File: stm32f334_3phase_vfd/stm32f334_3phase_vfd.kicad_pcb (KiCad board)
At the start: 2 copper layers, 120 x 70 mm, 65 parts, among them J1 HV, J2 PHA, J201 Conn_02x01, J202 Conn_02x01, J204 TP_IA, J205 Conn_02x01, J206 TP_VBU, J207 TP_VBV, J208 TP_VBW, J209 Conn_02x01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

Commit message: move 3 phase current sensors on a new board, allow for the current sense board to be stacked
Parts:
- removed C204, C213, C221: 100n, Capacitor_SMD:C_1206_3216Metric
- removed J204: TP_IA, Connector_PinHeader_2.54mm:PinHeader_1x01_P2.54mm_Vertical
- removed J211: TP_IB, Connector_PinHeader_2.54mm:PinHeader_1x01_P2.54mm_Vertical
- removed J217: TP_IC, Connector_PinHeader_2.54mm:PinHeader_1x01_P2.54mm_Vertical
- removed U202, U203, U204: CC6903SO-x0A, Package_SO:SO-8_3.9x4.9mm_P1.27mm
- added J10: MH, MountingHole:MountingHole_3.2mm_M3_Pad_TopBottom, F.Cu at (124.4, 103.2)
- added J11: MH, MountingHole:MountingHole_3.2mm_M3_Pad_TopBottom, F.Cu at (124.5, 41.2)
- added J12: Conn_01x06, Connector_JST:JST_PH_B6B-PH-K_1x06_P2.00mm_Vertical, F.Cu at (140.5, 93.6)
- C201, C203, C211, C212, C214, C215, C220, R202, R204, R206, R208, R211, R213: moved to B.Cu
- moved R203 213.3 mm to (150.8, 73.1), turned to 180 degrees
- moved C201 209.0 mm to (141.5, 75.5), turned to 180 degrees
- moved R205 207.3 mm to (150.8, 70.7), turned to 180 degrees
- moved R211 206.5 mm to (151.5, 62.9), turned to 180 degrees
- moved C203 205.6 mm to (141.5, 73.1), turned to 180 degrees
- moved J213 202.0 mm to (150.1, 53.5)
- moved R207 201.6 mm to (150.8, 66.6), turned to 180 degrees
- moved R204 201.0 mm to (151.5, 74.4), turned to 180 degrees
- moved C211 199.7 mm to (141.5, 70.7), turned to 180 degrees
- moved C215 197.5 mm to (141.5, 58.9), turned to 180 degrees
- moved R209 196.0 mm to (150.8, 64.2), turned to 180 degrees
- moved R208 195.3 mm to (151.5, 66.6), turned to 180 degrees
- moved C212 194.0 mm to (141.5, 66.6), turned to 180 degrees
- moved R210 192.2 mm to (155.7, 51.1), turned to 90 degrees
- moved R212 191.0 mm to (150.8, 61.8), turned to 180 degrees
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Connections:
- C205 pad 1: Net-(C205-Pad1) -> /power/OUTPUT_PH_W
- C207 pad 1: Net-(C207-Pad1) -> /power/OUTPUT_PH_V
- C209 pad 1: Net-(C209-Pad1) -> /power/OUTPUT_PH_U
- J2 pad 1: /power/OUTPUT_PHA -> /power/OUTPUT_PH_U
- J3 pad 1: /power/OUTPUT_PHB -> /power/OUTPUT_PH_V
- J4 pad 1: /power/OUTPUT_PHC -> /power/OUTPUT_PH_W
- U201 pad 21: Net-(C205-Pad1) -> /power/OUTPUT_PH_W
- U201 pad 22: Net-(C207-Pad1) -> /power/OUTPUT_PH_V
- U201 pad 23: Net-(C209-Pad1) -> /power/OUTPUT_PH_U
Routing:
- net GND: track 103.8 -> 2.17 mm, vias 3 -> 8
- net /power/3V3_ISENS: track 80.9 -> 0.00 mm, vias 3 -> 0
- net Net-(C205-Pad1): track 36.5 -> 0.00 mm, vias 2 -> 0
- net Net-(C209-Pad1): track 36.5 -> 0.00 mm, vias 2 -> 0
- net /CPU/ISENSE_C: track 36.1 -> 0.00 mm, vias 1 -> 0
- net Net-(C207-Pad1): track 33.7 -> 0.00 mm, vias 2 -> 0
- net /CPU/ISENSE_B: track 26.3 -> 0.00 mm, vias 1 -> 0
- net /power/VCC_15V: track 0.00 -> 16.1 mm
- net /power/OUTPUT_PHB: track 14.9 -> 0.00 mm
- net /power/OUTPUT_PHC: track 14.9 -> 0.00 mm
- net /power/OUTPUT_PHA: track 14.9 -> 0.00 mm
- net /CPU/ISENSE_A: track 14.8 -> 0.00 mm
- net /power/~{sd}_od: track 0.00 -> 14.3 mm
- net Net-(J201-Pad2): track 0.00 -> 7.34 mm
- net Net-(J215-Pad2): track 0.00 -> 7.32 mm
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- added copper zone on B.Cu, net /power/HV
- added copper zone on F.Cu, net /power/HV
- added copper zone on B.Cu, net /power/N
- added copper zone on B.Cu, net /power/OUTPUT_PH_U
- added copper zone on F.Cu, net /power/OUTPUT_PH_U
- added copper zone on B.Cu, net /power/OUTPUT_PH_V
- added copper zone on F.Cu, net /power/OUTPUT_PH_V
- added copper zone on B.Cu, net /power/OUTPUT_PH_W
- added copper zone on F.Cu, net /power/OUTPUT_PH_W
- added copper zone on B.Cu, net GND
- added copper zone on F.Cu, net GND
- removed copper zone on F.Cu, net /power/OUTPUT_PHA
- removed copper zone on F.Cu, net /power/OUTPUT_PHB
- removed copper zone on F.Cu, net /power/OUTPUT_PHC
- removed copper zone on F.Cu, net Net-(C205-Pad1)
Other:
- board text added: "A"
- board text added: "B"
- board text added: "C"
- board text added: "ES"
- board text added: "GND BOND POINT"
- board text added: "HIGH VOLTAGE"
- board text added: "HU"
- board text added: "HV"
- board text added: "HW"
- board text added: "LU"
- board text added: "LV"
- board text added: "LW"
- board text added: "POWER GND"
- board text added: "POWER VCC"

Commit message: switch to LQFP48 cpu, continue workin on layout
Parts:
- added C101: 8p, Capacitor_SMD:C_0805_2012Metric, F.Cu at (186.0, 75.4)
- added C102: 8p, Capacitor_SMD:C_0805_2012Metric, F.Cu at (188.9, 72.7)
- added C107: 100n, Capacitor_SMD:C_0805_2012Metric, F.Cu at (194.8, 57.0)
- added C108: 100n, Capacitor_SMD:C_0805_2012Metric, F.Cu at (194.9, 54.0)
- added C109: 100n, Capacitor_SMD:C_0805_2012Metric, F.Cu at (190.3, 59.8)
- added C110: 100n, Capacitor_SMD:C_0805_2012Metric, F.Cu at (190.3, 56.7)
- added C111: 100n, Capacitor_SMD:C_0805_2012Metric, F.Cu at (199.3, 54.0)
- added L101: FB, Inductor_SMD:L_0805_2012Metric, F.Cu at (190.4, 53.9)
- added U100: STM32F334C8Tx, Package_QFP:LQFP-48_7x7mm_P0.5mm, F.Cu at (174.4, 72.2)
- C202: value 330nF/630V -> B32774X8305K000; footprint Capacitor_THT:C_Rect_L24.0mm_W10.1mm_P22.50mm_MKT -> Capacitor_THT:C_Rect_L31.5mm_W11.0mm_P27.50mm_MKS4
- U101: value STM32F334K6Tx -> ECS-160-10-36-CKM-TR3; footprint Package_QFP:LQFP-32_7x7mm_P0.8mm -> Crystal:Crystal_SMD_2520-4Pin_2.5x2.0mm
- moved J207 215.5 mm to (142.4, 82.0), turned to 90 degrees
- moved J208 203.9 mm to (142.4, 78.4), turned to 90 degrees
- moved J206 201.0 mm to (142.4, 85.6), turned to 90 degrees
- moved U101 133.2 mm to (186.0, 72.7)
- moved J1 3.40 mm to (93.2, 89.5)
- moved J4 2.30 mm to (93.2, 62.7)
- moved J2 2.20 mm to (93.2, 75.2)
- moved C202 2.11 mm to (108.6, 58.6)
- moved R216 1.96 mm to (110.5, 54.1)
- moved C222 1.96 mm to (109.0, 47.3)
- moved R214 1.96 mm to (112.6, 48.8)
- moved R215 1.96 mm to (109.0, 44.8)
- moved R217 1.96 mm to (107.5, 50.3)
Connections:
- U101 pad 1: unconnected-(U101-Pad1) -> Net-(U100-Pad5)
- U101 pad 2: unconnected-(U101-Pad2) -> GND
- U101 pad 3: unconnected-(U101-Pad3) -> Net-(U100-Pad6)
- U101 pad 4: unconnected-(U101-Pad4) -> GND
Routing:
- net /CPU/L_V: track 0.00 -> 21.0 mm, vias 0 -> 1
- net /CPU/L_W: track 0.00 -> 19.5 mm
- net /CPU/H_U: track 0.00 -> 17.7 mm, vias 0 -> 1
- net /CPU/L_U: track 0.00 -> 15.1 mm
- net /CPU/H_V: track 0.00 -> 12.6 mm
- net /CPU/H_W: track 0.00 -> 12.3 mm, vias 0 -> 2
- net GND: track 2.17 -> 5.57 mm, vias 8 -> 18
- net GNDPWR: track 0.00 -> 2.91 mm
- net /power/Cin: track 42.0 -> 42.8 mm
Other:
- board text added: "VbU"
- board text added: "VbV"
- board text added: "VbW"

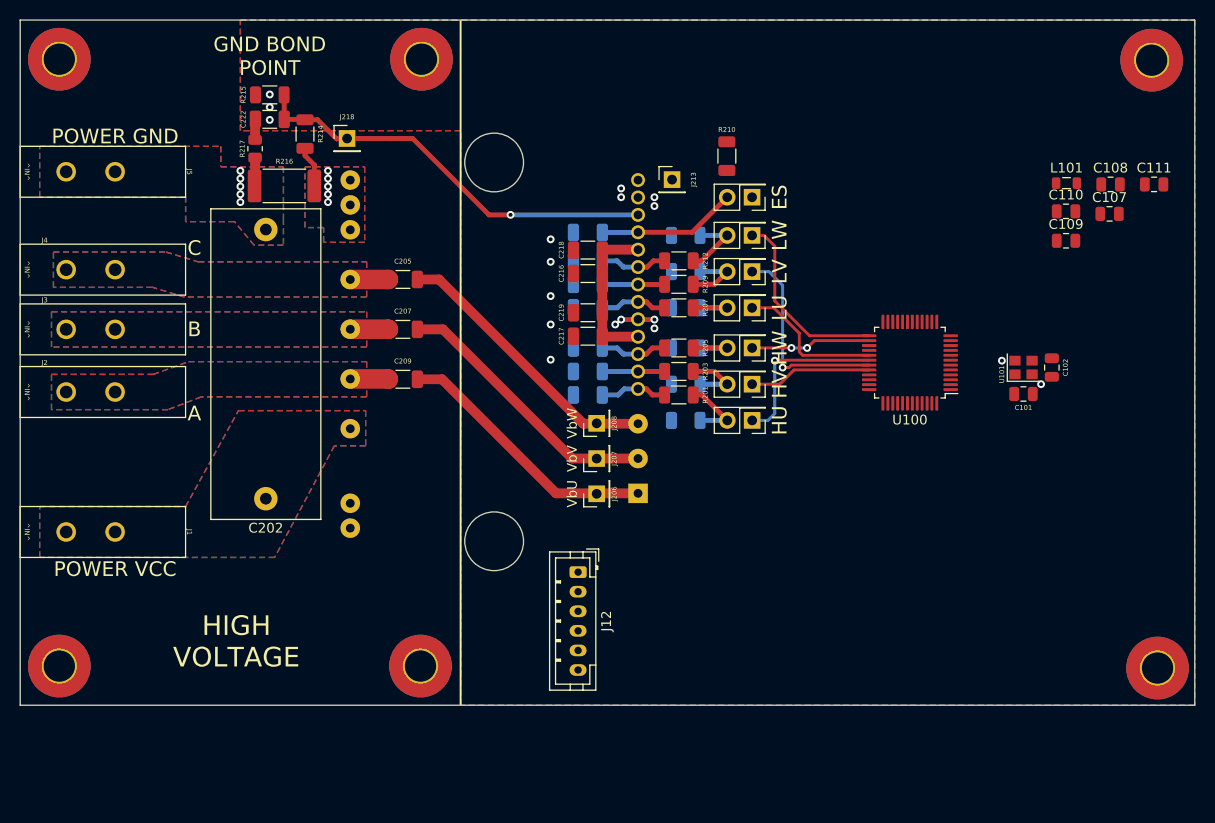
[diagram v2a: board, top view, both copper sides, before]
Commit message: pcb fix and schematic clean-up
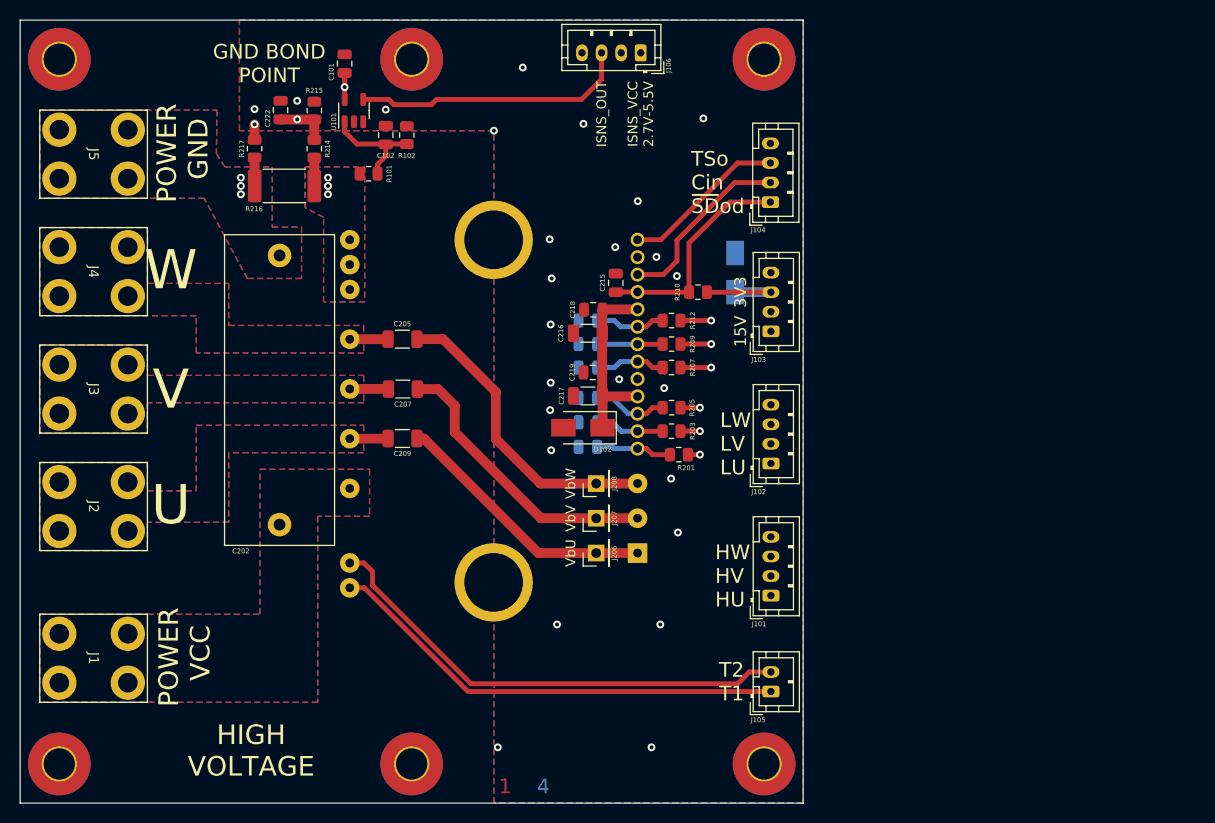
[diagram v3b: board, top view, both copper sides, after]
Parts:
- removed C107, C108, C109, C110, C111: 100n, Capacitor_SMD:C_0805_2012Metric
- removed J12: Conn_01x06, Connector_JST:JST_PH_B6B-PH-K_1x06_P2.00mm_Vertical
- removed J201, J202, J205, J209, J212, J214, J215: Conn_02x01, Connector_PinHeader_2.54mm:PinHeader_2x01_P2.54mm_Vertical
- removed J213: TP_TSO, Connector_PinHeader_2.54mm:PinHeader_1x01_P2.54mm_Vertical
- removed J218: TP_CSENSE, Connector_PinHeader_2.54mm:PinHeader_1x01_P2.54mm_Vertical
- removed L101: FB, Inductor_SMD:L_0805_2012Metric
- removed R202, R204, R206, R208, R211, R213: 10k, Resistor_SMD:R_1206_3216Metric
- removed U100: STM32F334C8Tx, Package_QFP:LQFP-48_7x7mm_P0.5mm
- added D101: D, Diode_SMD:D_SMA, B.Cu at (156.6, 63.0)
- added D102: D, Diode_SMD:D_SMA, F.Cu at (141.0, 78.8)
- added J101: Conn_01x04, Connector_JST:JST_PH_B4B-PH-K_1x04_P2.00mm_Vertical, F.Cu at (160.2, 96.0)
- added J102: Conn_01x04, Connector_JST:JST_PH_B4B-PH-K_1x04_P2.00mm_Vertical, F.Cu at (160.2, 82.5)
- added J103: Conn_01x04, Connector_JST:JST_PH_B4B-PH-K_1x04_P2.00mm_Vertical, F.Cu at (160.2, 69.0)
- added J104: Conn_01x04, Connector_JST:JST_PH_B4B-PH-K_1x04_P2.00mm_Vertical, F.Cu at (160.2, 55.8)
- added J105: Conn_01x02, Connector_JST:JST_PH_B2B-PH-K_1x02_P2.00mm_Vertical, F.Cu at (160.2, 105.8)
- added J106: Conn_01x04, Connector_JST:JST_PH_B4B-PH-K_1x04_P2.00mm_Vertical, F.Cu at (146.9, 40.5)
- added R101: 1k, Resistor_SMD:R_0805_2012Metric, F.Cu at (119.1, 52.9)
- added R102: 1k, Resistor_SMD:R_0805_2012Metric, F.Cu at (123.0, 49.0)
- C101: value 8p -> 100n
- C102: value 8p -> 10p
- C201, C203, C211, C212, C214, C218, C219, C220, C222: footprint Capacitor_SMD:C_1206_3216Metric -> Capacitor_SMD:C_0805_2012Metric
- C215: footprint Capacitor_SMD:C_1206_3216Metric -> Capacitor_SMD:C_0805_2012Metric; moved to F.Cu
- J1, J2, J3, J4, J5: footprint stm32f334_3phase_vfd:1904969 -> stm32f334_3phase_vfd:KEYSTONE_7788
- R201, R203, R205, R207, R209, R210, R212, R214, R215: footprint Resistor_SMD:R_1206_3216Metric -> Resistor_SMD:R_0805_2012Metric
- U101: value ECS-160-10-36-CKM-TR3 -> INA180B1; footprint Crystal:Crystal_SMD_2520-4Pin_2.5x2.0mm -> Package_TO_SOT_SMD:SOT-23-5
- moved C101 77.1 mm to (116.7, 41.6), turned to 90 degrees
- moved U101 73.3 mm to (117.6, 46.5), turned to 90 degrees
- moved C102 72.1 mm to (120.8, 49.0), turned to 90 degrees
- moved J8 41.4 mm to (159.5, 113.2)
- moved J9 39.6 mm to (159.5, 41.2)
- moved R210 14.2 mm to (152.8, 65.0), turned to 0 degrees
- moved J1 13.1 mm to (91.0, 102.4)
- moved J2 11.9 mm to (91.0, 86.9)
- moved J10 10.0 mm to (123.5, 113.2)
- moved J6 10.0 mm to (87.5, 113.2)
- moved J3 6.48 mm to (91.0, 74.9)
- moved J208 6.15 mm to (142.3, 84.5)
- moved R203 6.15 mm to (150.1, 79.2)
- moved R207 6.15 mm to (150.1, 72.7)
- moved R212 6.15 mm to (150.1, 67.9)
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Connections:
- net /power/OUTPUT_PH_U renamed /power/U
- net /power/OUTPUT_PH_V renamed /power/V
- net /power/OUTPUT_PH_W renamed /power/W
- C101 pad 1: GND -> /power/ISENSE_VCC
- C101 pad 2: Net-(U100-Pad5) -> GND
- C102 pad 1: Net-(U100-Pad6) -> Net-(C102-Pad1)
- R201 pad 1: Net-(J201-Pad2) -> /power/HinU
- R203 pad 1: Net-(J202-Pad2) -> /power/HinV
- R205 pad 1: Net-(J205-Pad2) -> /power/HinW
- R207 pad 1: Net-(J209-Pad2) -> /power/LinU
- R209 pad 1: Net-(J212-Pad2) -> /power/LinV
- R212 pad 1: Net-(J215-Pad2) -> /power/LinW
- U101 pad 1: Net-(U100-Pad5) -> Net-(C102-Pad1)
- U101 pad 3: Net-(U100-Pad6) -> GND
- U101 pad 4: GND -> /power/ISENSE_OUT
- U201 pad 25: /CPU/TSENSE_2 -> /power/T2
- U201 pad 26: /CPU/TSENSE_1 -> /power/T1
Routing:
- net /power/T2: track 0.00 -> 49.5 mm
- net /power/T1: track 0.00 -> 47.4 mm
- net /power/ISENSE_VCC: track 0.00 -> 35.8 mm, vias 0 -> 1
- net /power/ISENSE_OUT: track 0.00 -> 28.3 mm
- net /power/Cin: track 42.8 -> 68.1 mm
- net /power/HinW: track 0.00 -> 22.0 mm, vias 0 -> 1
- net /power/HinV: track 0.00 -> 21.8 mm, vias 0 -> 1
- net /CPU/L_V: track 21.0 -> 0.00 mm, vias 1 -> 0
- net /power/HinU: track 0.00 -> 20.7 mm, vias 0 -> 1
- net /CPU/L_W: track 19.5 -> 0.00 mm
- net /power/LinV: track 0.00 -> 17.8 mm, vias 0 -> 1
- net /power/LinW: track 0.00 -> 17.7 mm, vias 0 -> 1
- net /power/VCC_15V: track 16.1 -> 33.9 mm
- net /power/LinU: track 0.00 -> 17.7 mm, vias 0 -> 1
- net /CPU/H_U: track 17.7 -> 0.00 mm, vias 1 -> 0
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- added copper zone on In1.Cu, net /power/HV
- added copper zone on In2.Cu, net /power/HV
- added copper zone on In1.Cu, net /power/N
- added copper zone on In2.Cu, net /power/N
- added copper zone on In1.Cu, net /power/U
- added copper zone on In2.Cu, net /power/U
- added copper zone on In1.Cu, net /power/V
- added copper zone on In2.Cu, net /power/V
- added copper zone on In1.Cu, net /power/W
- added copper zone on In2.Cu, net /power/W
- added copper zone on In1.Cu, net GND
- added copper zone on In2.Cu, net GND
- added copper zone on In1.Cu, net GNDPWR
- added copper zone on In2.Cu, net GNDPWR
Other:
- board size 120 x 70 mm -> 80 x 80 mm
- copper layers 2 -> 4
- board text added: "1"
- board text added: "15V"
- board text added: "2"
- board text added: "3"
- board text added: "3V3"
- board text added: "4"
- board text added: "HW HV HU"
- board text added: "ISNS_OUT"
- board text added: "ISNS_VCC 2.7V-5.5V"
- board text added: "LW LV LU"
- board text added: "T2 T1"
- board text added: "TSo Cin ~{SD}od"
- board text added: "U"
- board text added: "V"
- board text added: "W"
- board text removed: "A"
- board text removed: "B"
- board text removed: "C"
- board text removed: "ES"
- board text removed: "HU"
- board text removed: "HV"
- board text removed: "HW"
- board text removed: "LU"
- board text removed: "LV"
- board text removed: "LW"
